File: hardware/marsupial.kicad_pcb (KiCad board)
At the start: 4 copper layers, 53.1 x 98 mm, 208 parts, among them J101 DC IN, J102 DC OUT, J103 FPC, J201 USB_C_Receptacle_USB2.0, J301 MANUAL, J401 TagConnect, J501 MANUAL, J601 USB_C_Receptacle_USB2.0, J701 USB_C_Receptacle_USB2.0, Q201 DMP3028, Q202 DMP3028, Q203 DMP3028, Q204 MMBT3904, Q205 MMBT3904, Q206 DMP3028, Q207 MMBT3904, Q401 AO3400A, Q402 AO3400A, Q601 DMP3028, Q602 DMP3028, Q603 DMP3028, Q604 MMBT3904, Q605 MMBT3904, Q606 DMP3028, Q607 MMBT3904, SW1 RESET, U101 HT7550-1, U102 XC6206, U201 SRV05-4, U202 INA381A2IDSGR, U203 BL1551B, U301 SiC437, U401 STM32G071RBTx, U501 SiC437, U601 SRV05-4, U602 INA381A2IDSGR, U603 BL1551B, U701 USB2412-DZK-TR, Y401 12MHz, Y701 24MHz

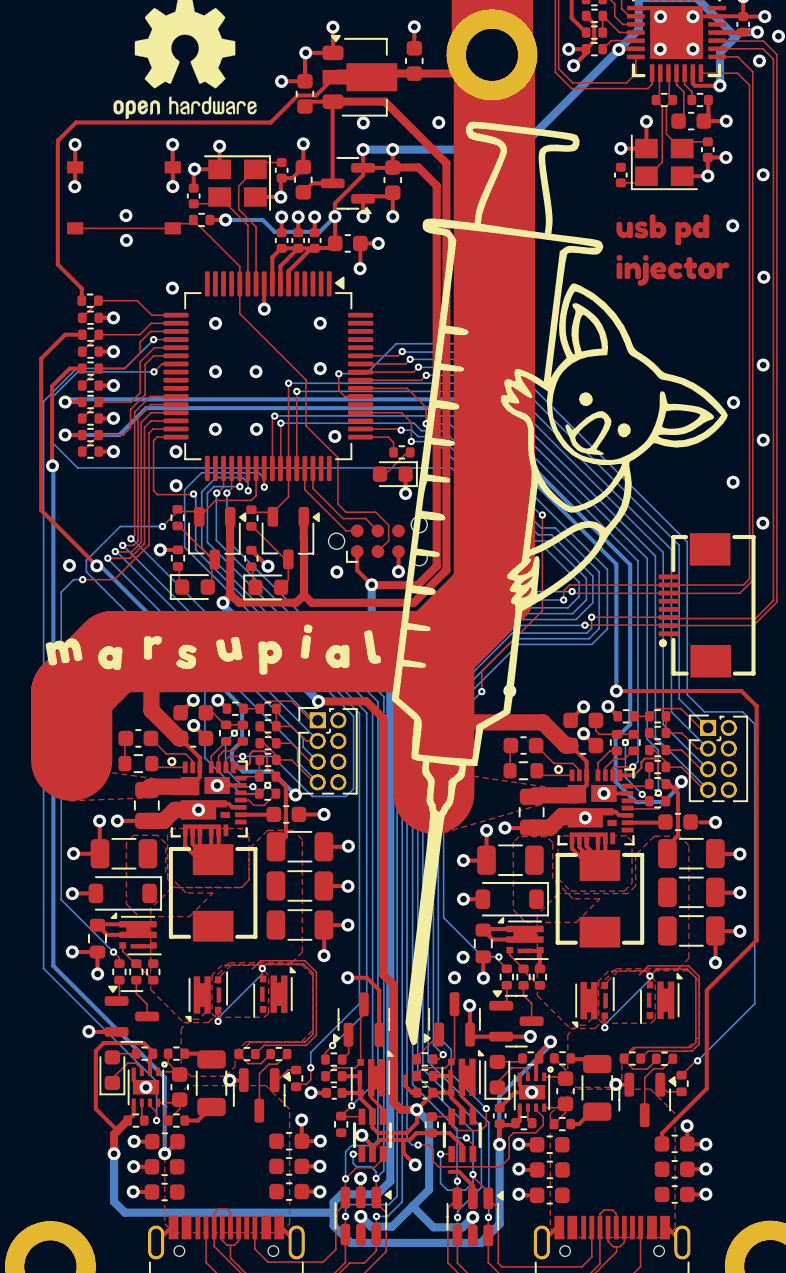
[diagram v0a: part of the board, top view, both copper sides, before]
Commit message: change to C8U3 variant
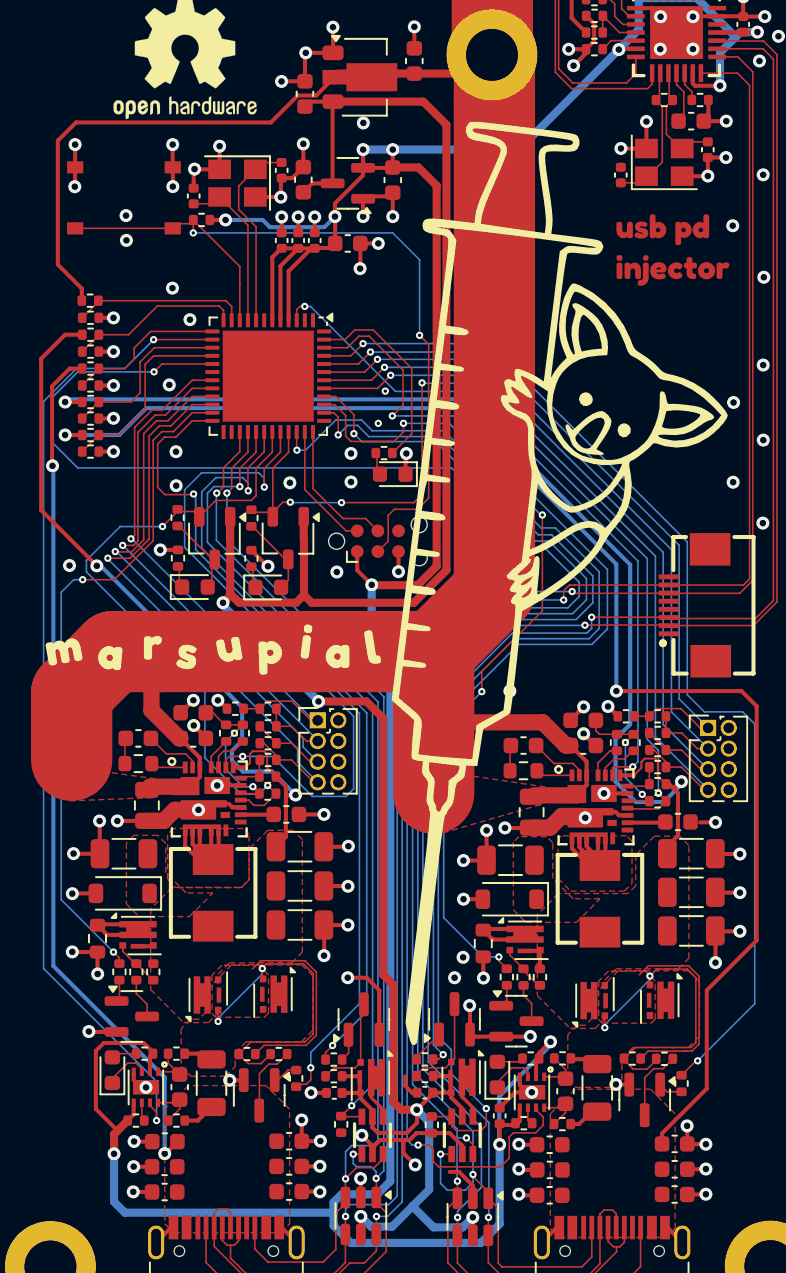
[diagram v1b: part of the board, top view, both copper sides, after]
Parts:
- PCB1: renamed from FC_; value Val_ -> PCB
- R303, R503: value 499k -> 200k
- U401: value STM32G071RBTx -> STM32G071C8Ux; footprint Package_QFP:LQFP-64_10x10mm_P0.5mm -> Package_DFN_QFN:QFN-48-1EP_7x7mm_P0.5mm_EP5.6x5.6mm
- moved R412 1.10 mm to (136.2, 92.3), turned to 180 degrees
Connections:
- R412 pad 1: Net-(U401-PC9) -> Net-(U401-PB8)
- U401 pad 10: /MCU/XIN -> /MCU/~{RST}
- U401 pad 11: /MCU/XOUT -> /MCU/VIN
- U401 pad 12: /MCU/~{RST} -> /MCU/VBUS1
- U401 pad 13: unconnected-(U401-PC0-Pad13) -> /MCU/VOUT1
- U401 pad 14: unconnected-(U401-PC1-Pad14) -> /MCU/UCPD1_ISENSE
- U401 pad 15: unconnected-(U401-PC2-Pad15) -> /MCU/VBUS2
- U401 pad 16: unconnected-(U401-PC3-Pad16) -> /MCU/VOUT2
- U401 pad 17: /MCU/VIN -> /MCU/UCPD2_ISENSE
- U401 pad 18: /MCU/VBUS1 -> unconnected-(U401-PA7-Pad18)
- U401 pad 19: /MCU/VOUT1 -> /MCU/UCPD1_PDO2
- U401 pad 20: /MCU/UCPD1_ISENSE -> /MCU/UCPD1_PDO3
- U401 pad 21: /MCU/VBUS2 -> /MCU/UCPD1_PDO4
- U401 pad 22: /MCU/VOUT2 -> /MCU/UCPD1_PDO5
- U401 pad 23: /MCU/UCPD2_ISENSE -> /MCU/UCPD1_VBUS_DISCHG
- U401 pad 24: unconnected-(U401-PA7-Pad24) -> /MCU/UCPD1_SRC_EN
- U401 pad 27: /MCU/UCPD1_PDO2 -> /UCPD1_SRC/CC2
- U401 pad 28: /MCU/UCPD1_PDO3 -> /UCPD1_SRC/CC1
- U401 pad 29: /MCU/UCPD1_PDO4 -> /MCU/VCONN1_SEL
- U401 pad 3: unconnected-(U401-PC13-Pad3) -> /MCU/DCDC2_EN
- U401 pad 30: /MCU/UCPD1_PDO5 -> /MCU/VCONN1_EN
- U401 pad 31: /MCU/UCPD1_VBUS_DISCHG -> /MCU/DCDC1_PGOOD
- U401 pad 32: /MCU/UCPD1_SRC_EN -> /MCU/DCDC1_EN
- U401 pad 33: unconnected-(U401-PB13-Pad33) -> /MCU/DCDC2_PGOOD
- U401 pad 34: unconnected-(U401-PB14-Pad34) -> /MCU/VCONN2_EN
- U401 pad 35: /UCPD1_SRC/CC2 -> /MCU/SWDIO
- U401 pad 36: /UCPD1_SRC/CC1 -> /MCU/SWCLK
- U401 pad 37: /MCU/VCONN1_SEL -> unconnected-(U401-PA15-Pad37)
- U401 pad 38: /MCU/VCONN1_EN -> /UCPD2_SRC/CC1
- U401 pad 39: /MCU/DCDC1_PGOOD -> /MCU/UCPD2_VBUS_DISCHG
- U401 pad 4: unconnected-(U401-PC14-Pad4) -> +3V3
- U401 pad 40: /MCU/DCDC1_EN -> /UCPD2_SRC/CC2
- U401 pad 41: /MCU/VCONN2_SEL -> /MCU/UCPD2_PDO5
- U401 pad 42: /MCU/VCONN2_EN -> /MCU/UCPD2_PDO4
- U401 pad 43: /MCU/DCDC2_PGOOD -> /MCU/UCPD2_PDO3
- U401 pad 44: /MCU/DCDC2_EN -> /MCU/UCPD2_PDO2
- U401 pad 45: /MCU/SWDIO -> /MCU/UCPD2_SRC_EN
- U401 pad 46: /MCU/SWCLK -> /MCU/VCONN2_SEL
- U401 pad 47: unconnected-(U401-PA15-Pad47) -> Net-(U401-PB8)
- U401 pad 49: Net-(U401-PC9) -> GND
- U401 pad 5: unconnected-(U401-PC15-Pad5) -> +3V3
- U401 pad 7: +3V3 -> GND
- U401 pad 8: +3V3 -> /MCU/XIN
- U401 pad 9: GND -> /MCU/XOUT
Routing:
- net /MCU/~{RST}: track 34.2 -> 50.1 mm, vias 0 -> 2
- net Net-(U401-PB8): track 0.00 -> 12.3 mm
- net +3V3: track 221.4 -> 227.9 mm
- net /MCU/DCDC2_PGOOD: track 54.6 -> 60.2 mm, vias 2 -> 4
- net /MCU/VBUS1: track 6.50 -> 10.6 mm
- net /MCU/VIN: track 6.60 -> 10.7 mm
- net /UCPD2_SRC/CC1: track 82.5 -> 86.3 mm
- net /MCU/UCPD2_VBUS_DISCHG: track 47.6 -> 50.8 mm
- net Net-(U401-PC9): track 2.78 -> 0.00 mm
- net /UCPD2_SRC/CC2: track 86.3 -> 89.0 mm
- net /UCPD1_SRC/CC2: track 64.2 -> 66.9 mm
- net /MCU/VCONN1_EN: track 45.4 -> 48.0 mm
- net /MCU/DCDC1_PGOOD: track 37.7 -> 40.3 mm
- net /MCU/DCDC1_EN: track 39.5 -> 42.1 mm
- net /UCPD1_SRC/CC1: track 70.6 -> 73.3 mm
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
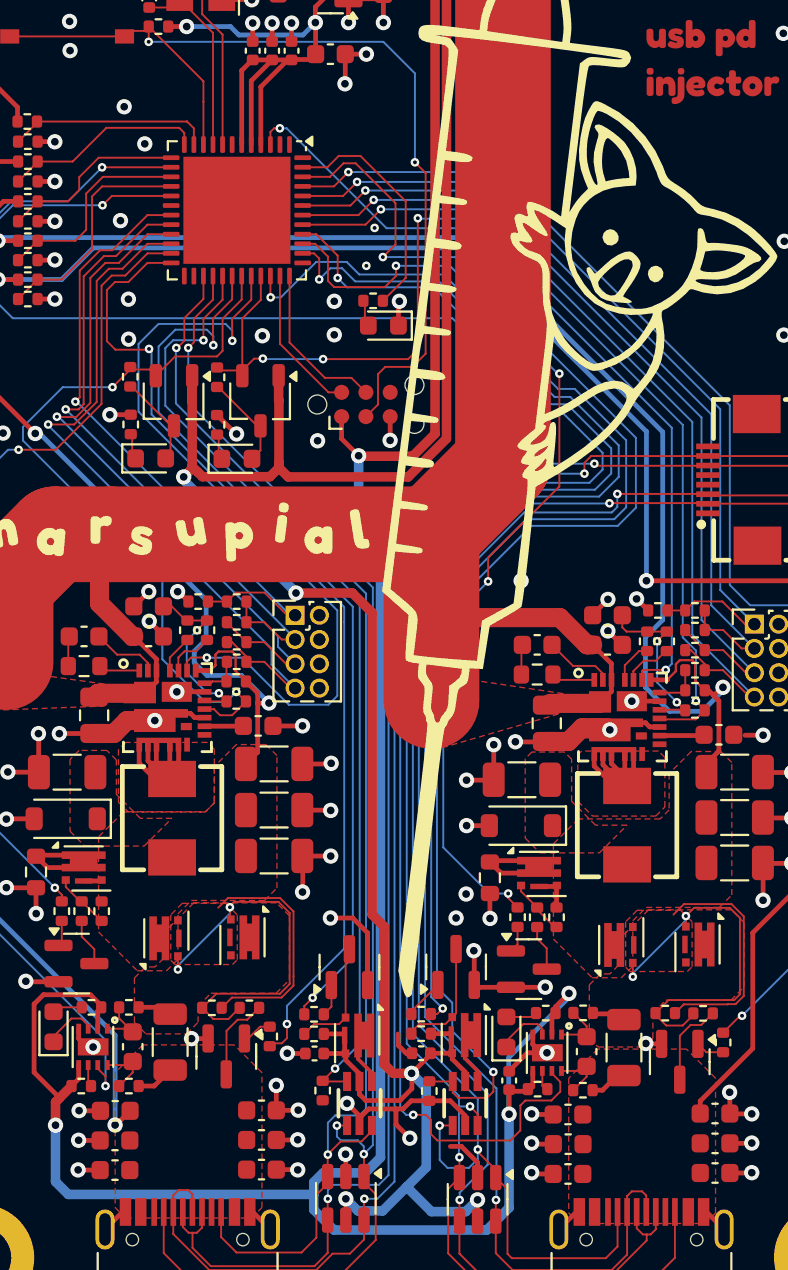
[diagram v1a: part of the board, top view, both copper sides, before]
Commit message: fix pinout issues hw rev 1
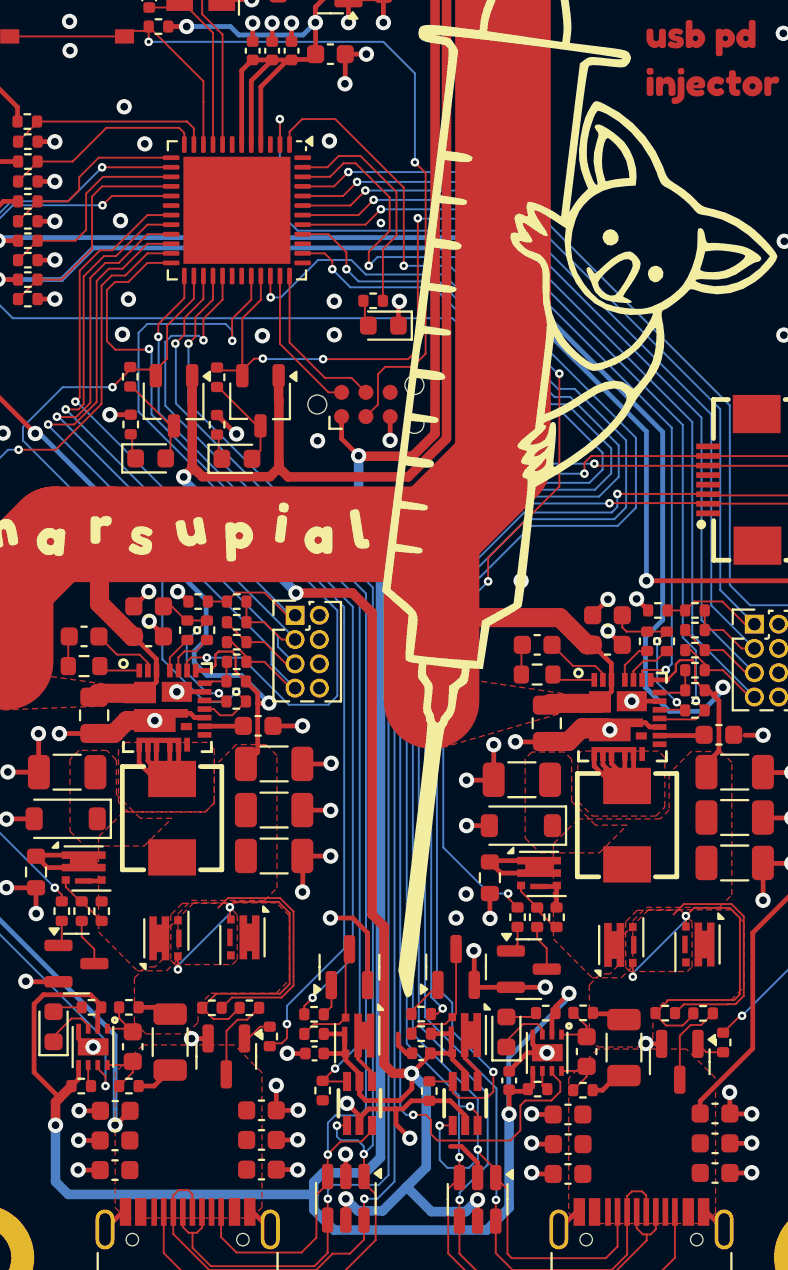
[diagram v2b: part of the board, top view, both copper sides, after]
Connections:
- U401 pad 1: unconnected-(U401-PC13-Pad1) -> /MCU/UCPD2_VBUS_DISCHG
- U401 pad 2: unconnected-(U401-PC14-Pad2) -> /MCU/DCDC2_EN
- U401 pad 25: unconnected-(U401-PB13-Pad25) -> /MCU/VCONN1_EN
- U401 pad 26: unconnected-(U401-PB14-Pad26) -> /MCU/DCDC1_PGOOD
- U401 pad 3: /MCU/DCDC2_EN -> unconnected-(U401-PC15-Pad3)
- U401 pad 30: /MCU/VCONN1_EN -> unconnected-(U401-PC6-Pad30)
- U401 pad 31: /MCU/DCDC1_PGOOD -> unconnected-(U401-PC7-Pad31)
- U401 pad 38: /UCPD2_SRC/CC1 -> /UCPD2_SRC/CC2
- U401 pad 39: /MCU/UCPD2_VBUS_DISCHG -> unconnected-(U401-PD1-Pad39)
- U401 pad 40: /UCPD2_SRC/CC2 -> /UCPD2_SRC/CC1
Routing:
- net /MCU/UCPD2_VBUS_DISCHG: track 50.8 -> 55.6 mm
- net /MCU/VCONN1_EN: track 48.0 -> 44.4 mm
- net /MCU/DCDC2_EN: track 42.7 -> 45.9 mm
- net /MCU/DCDC1_PGOOD: track 40.3 -> 38.0 mm
- net /MCU/VCONN2_SEL: track 72.8 -> 74.2 mm
- net /UCPD2_SRC/CC2: track 89.0 -> 88.1 mm
